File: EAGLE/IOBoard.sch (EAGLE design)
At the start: 71 parts, among them IC1 MEGA32-P, IC2 MAX232, IC3 ADM803SAKS, K1 HE3321, K2 HE3321, K3 HE3321, K4 HE3321, K5 HE3321, K6 HE3321, K7 HE3321, K8 HE3321, T1 NDS351AN, T2 NDS351AN, T3 NDS351AN, T4 NDS351AN, T5 NDS351AN, T6 NDS351AN, T7 NDS351AN, T8 NDS351AN

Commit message: -
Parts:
- removed D1, D2, D3, D4, D5, D6, D7, D8: 1N4148, diode:1N4148DO35-10
- removed IC2: MAX232, maxim:MAX232
- removed IC3: ADM803SAKS, memmert_joerg:ADM803SAKS
- removed K1, K2, K3, K4, K5, K6, K7, K8: HE3321, relay:HE3321
- removed OK1, OK2, OK3, OK4, OK5, OK6, OK7, OK8: SFH6206, optocoupler:SFH6206
- removed R10, R11, R12, R13, R14, R15, R16: 374, rcl:R-EU_0207/10
- removed T1, T2, T3, T4, T5, T6, T7, T8: NDS351AN, memmert_joerg:NDS351AN
- removed X1, X10, X11, X12, X13, X14, X15, X16, X2, X3, X4, X5, X6, X7, X8, X9: (no value), con-phoenix-500:MSTBV2
- removed X17: (no value), con-subd:F09H
- added 3V3, BAT: (no value), pinhead:PINHD-1X2
- added C3, C4, C5: 100n, rcl:C-EUC0805
- added C6, C7, C8, C9: 20p, rcl:C-EUC0805
- added JP1: (no value), pinhead:PINHD-1X9
- added JP10, JP11, JP2, JP3, JP4, JP5, JP6, JP7, JP8, JP9: JUMPER_SMALL, memmert_joerg:JUMPER_SMALL
- added JTAG: (no value), con-harting-ml:ML20
- added LED1, LED2, LED3, LED4: (no value), led:LEDSML0603
- added Q2: 32kHz, crystal:MC-306
- added S1: COMBICON_1803442, memmert_joerg:COMBICON_1803442
- added U1: STM32F10XRXT6, stm32:STM32F10XRXT6
- C1, C2: value (none) -> 100n; device rcl:C-EU025_050-025X075 -> rcl:C-EUC0805
- IC1: value MEGA32-P -> TPS61097; device atmel:MEGA32-P -> spfennig:TPS61097
- Q1: value (none) -> 8MHz; device memmert_joerg:CRYSTALHC49S -> crystal:CSM-7X-DU
- R1: value 5k -> 390; device rcl:R-EU_0207/10 -> rcl:R-EU_R0805
- R2, R3, R4: value 5k -> 10k; device rcl:R-EU_0207/10 -> rcl:R-EU_R0805
- R5: value 5k -> 0; device rcl:R-EU_0207/10 -> rcl:R-EU_R0805
- R6, R7, R8: value 5k -> 500; device rcl:R-EU_0207/10 -> rcl:R-EU_R0805
- R9: value 374 -> 500; device rcl:R-EU_0207/10 -> rcl:R-EU_R0805
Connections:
- removed net IN0: IC1.(ADC0)PA0, OK1.C, R1.1
- removed net IN1: IC1.(ADC1)PA1, OK2.C, R2.1
- removed net IN2: IC1.(ADC2)PA2, OK3.C, R3.1
- removed net IN3: IC1.(ADC3)PA3, OK4.C, R4.1
- removed net IN4: IC1.(ADC4)PA4, OK5.C, R5.1
- removed net IN5: IC1.(ADC5)PA5, OK6.C, R6.1
- removed net IN6: IC1.(ADC6)PA6, OK7.C, R7.1
- removed net IN7: IC1.(ADC7)PA7, OK8.C, R8.1
- removed net N$15: OK3.AC1, R11.2
- removed net N$16: C2.2, IC2G$1.C2-
- removed net N$17: R13.1, X5-1.SK
- removed net N$18: OK5.AC2, X5-2.SK
- removed net N$19: D1.A, K11.2, T1.D
- removed net N$20: OK5.AC1, R13.2
- removed net N$21: R14.1, X6-1.SK
- removed net N$22: OK6.AC2, X6-2.SK
- removed net N$23: IC1.RESET, IC3.!RESET
- removed net N$24: OK6.AC1, R14.2
- removed net N$25: R15.1, X7-1.SK
- removed net N$26: OK7.AC2, X7-2.SK
- removed net N$27: D4.A, K21.2, T2.D
- removed net N$28: OK7.AC1, R15.2
- removed net N$29: R16.1, X8-1.SK
- removed net N$30: OK8.AC2, X8-2.SK
- removed net N$31: D5.A, K31.2, T3.D
- removed net N$32: OK8.AC1, R16.2
- removed net N$33: D7.A, K41.2, T4.D
- removed net N$34: D2.A, K51.2, T5.D
- removed net N$35: D3.A, K61.2, T6.D
- removed net N$36: D8.A, K81.2, T8.D
- removed net N$37: D6.A, K71.2, T7.D
- removed net N$38: K12.S, X9-2.SK
- removed net N$39: K12.P, X9-1.SK
- removed net N$40: K22.S, X10-2.SK
- removed net N$41: K22.P, X10-1.SK
- removed net N$42: K32.S, X11-2.SK
- removed net N$43: K32.P, X11-1.SK
- removed net N$44: K42.S, X12-2.SK
- removed net N$45: K42.P, X12-1.SK
- removed net N$46: K82.S, X16-2.SK
- removed net N$47: K82.P, X16-1.SK
- removed net N$48: K72.P, X15-1.SK
- removed net N$49: K72.S, X15-2.SK
- removed net N$50: K62.P, X14-1.SK
- removed net N$51: K62.S, X14-2.SK
- removed net N$52: K52.P, X13-1.SK
- removed net N$53: K52.S, X13-2.SK
- removed net N$54: IC2G$1.T2OUT, X17.3
- removed net N$55: IC2G$1.R1IN, X17.2
- removed net N$56: IC1.XTAL2, Q1.2
- removed net N$57: IC1.XTAL1, Q1.1
- removed net OUT0: IC1.(T0/XCK)PB0, T1.G
- removed net OUT1: IC1.(T1)PB1, T2.G
- removed net OUT2: IC1.(AIN0/INT2)PB2, T3.G
- removed net OUT3: IC1.(AIN1/OC0)PB3, T4.G
- removed net OUT4: IC1.(SS)PB4, T5.G
- removed net OUT5: IC1.(MOSI)PB5, T6.G
- removed net OUT6: IC1.(MISO)PB6, T7.G
- removed net OUT7: IC1.(SCK)PB7, T8.G
- removed net RXUART: IC1.(RXD)PD0
- removed net TCK: IC1.(TCK)PC2
- removed net TDI: IC1.(TDI)PC5
- removed net TDO: IC1.(TDO)PC4
- removed net TMS: IC1.(TMS)PC3
- removed net TXUART: IC1.(TXD)PD1
- removed net VCC: D1.C, D2.C, D3.C, D4.C, D5.C, D6.C, D7.C, D8.C, IC1.AREF, IC1.AVCC, IC1.VCC, IC2G$1.V+, IC3.VCC, K11.1, K21.1, K31.1, K41.1, K51.1, K61.1, K71.1, K81.1, R1.2, R2.2, R3.2, R4.2, R5.2, R6.2, R7.2, R8.2
- new net +3V3: 3V3.1, C1.2, C2.2, C3.2, C4.2, IC1.VOUT, JP1.2, JP1.9, JP10.2, JP8.2, JTAG.1, JTAG.2, S1.3, U1AN_POWER.VBAT, U1AN_POWER.VDDA, U1POWER.VDD_1, U1POWER.VDD_2, U1POWER.VDD_3, U1POWER.VDD_4
- new net BAT+: BAT.1, IC1.EN, IC1.VIN
- new net BAT-: BAT.2, IC1.GND
- new net BOOT0: JP10.1, JP11.1, U1RESET.BOOT0
- new net BOOT1: JP8.1, JP9.1, U1PORTB_L.PB2
- new net JTAG_DBGACK: JTAG.19, R4.2
- new net JTAG_DBGRQ: JTAG.17, R3.2
- new net JTAG_NSRST: JP7.2, JTAG.15
- new net JTAG_NTRST: JP3.2, JTAG.3
- new net JTAG_RTCK: JTAG.11, R2.2
- new net JTAG_TCK: JP4.2, JTAG.9
- new net JTAG_TDI: JP5.2, JTAG.5
- new net JTAG_TDO: JP2.2, JTAG.13
- new net JTAG_TMS: JP6.2, JTAG.7
- new net LCD_CS: JP1.7, U1PORTB_L.PB6
- new net LCD_D/C: JP1.5, U1PORTA_H.PA8
- new net LCD_MISO: JP1.1, U1PORTA_L.PA6
- new net LCD_MOSI: JP1.4, U1PORTA_L.PA7
- new net LCD_RESET: JP1.6, U1PORTC_L.PC7
- new net LCD_SCK: JP1.3, U1PORTA_L.PA5
- new net OSC_RTC_IN: C8.1, Q2.2, U1PORTB_H.PB14
- new net OSC_RTC_OUT: R5.1, U1PORTB_H.PB15
- new net SERIAL1_RX: S1.2, U1PORTA_H.PA10
- new net SERIAL1_TX: S1.1, U1PORTA_H.PA9
- new net TEST_1: LED1.A, U1PORTA_L.PA3
- new net TEST_2: LED2.A, U1PORTA_L.PA2
- new net TEST_3: LED3.A, U1PORTA_L.PA1
- new net TEST_4: LED4.A, U1PORTA_L.PA0
- net GND: now also 3V3.2, C1.1, C2.1, C3.1, C4.1, C5.2, C6.2, C7.1, C8.2, C9.1, JP1.8, JP11.2, JP9.2, JTAG.10, JTAG.12, JTAG.14, JTAG.16, JTAG.18, JTAG.20, JTAG.4, JTAG.6, JTAG.8, R2.1, R3.1, R4.1, R6.1, R7.1, R8.1, R9.1, S1.4, U1AN_POWER.VSSA, U1POWER.VSS_1, U1POWER.VSS_2, U1POWER.VSS_3, U1POWER.VSS_4; no longer IC1.GND, IC1.GND@1, IC2G$1.V-, IC3.GND, OK1.E, OK2.E, OK3.E, OK4.E, OK5.E, OK6.E, OK7.E, OK8.E, T1.S, T2.S, T3.S, T4.S, T5.S, T6.S, T7.S, T8.S, X17.5
- net N$1: now also C5.1, JP7.1, U1RESET.NRST; no longer R9.1, X1-1.SK
- net N$10: now also C9.2, Q2.1, R5.2; no longer OK4.AC2, X4-2.SK
- net N$11: now also LED1.C, R6.2; no longer C2.1, IC2G$1.C2+
- net N$12: now also LED2.C, R7.2; no longer OK3.AC2, X3-2.SK
- net N$13: now also LED3.C, R8.2; no longer R12.1, X4-1.SK
- net N$14: now also LED4.C, R9.2; no longer OK4.AC1, R12.2
- net N$2: now also C6.1, Q1.2, U1PORTD/OSC.PD0/OSC<=; no longer OK1.AC1, R9.2
- net N$3: now also R1.1, U1PORTD/OSC.PD1/OSC=>; no longer C1.1, IC2G$1.C1+
- net N$4: now also JP2.1, U1PORTB_L.PB3; no longer OK1.AC2, X1-2.SK
- net N$5: now also C7.2, Q1.1, R1.2; no longer R10.1, X2-1.SK
- net N$6: now also JP4.1, U1PORTA_H.PA14; no longer OK2.AC1, R10.2
- net N$7: now also JP6.1, U1PORTA_H.PA13; no longer OK2.AC2, X2-2.SK
- net N$8: now also JP5.1, U1PORTA_H.PA15; no longer C1.2, IC2G$1.C1-
- net N$9: now also JP3.1, U1PORTB_L.PB4; no longer R11.1, X3-1.SK
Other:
- note added: "JTAG"
- note added: "STM32F103"
- note removed: "Input / Output"
- note removed: "Input Ports"
- note removed: "MCU"
- note removed: "Output Ports"
- note removed: "UART -> RS232"

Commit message: -
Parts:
- added C10, C11: 10u, rcl:C-EUC0805
- added L2: 4u7, ipc-7351-inductor:INDUCTOR_2520
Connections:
- new net N$15: IC1.L, L2.2
- net +3V3: now also C11.2
- net BAT+: now also C10.2, L2.1
- net BAT-: now also C10.1
- net GND: now also C11.1
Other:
- moved on the sheet: IC1
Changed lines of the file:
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@@
 <layer number="97" name="Info" color="7" fill="1" visible="yes" active="yes"/>
 <layer number="98" name="Guide" color="6" fill="1" visible="yes" active="yes"/>
+<layer number="99" name="SpiceOrder" color="5" fill="1" visible="yes" active="yes"/>
 <layer number="100" name="Muster" color="7" fill="1" visible="no" active="no"/>
 <layer number="101" name="Patch_Top" color="12" fill="4" visible="yes" active="yes"/>
@@
 </variantdefs>
 <classes>
-<class number="0" name="default" width="0" drill="0">
+<class number="0" name="default" width="0.2" drill="0.4">
+<clearance class="0" value="0.2"/>
 </class>
 </classes>
@@
 <part name="IC1" library="spfennig" deviceset="TPS61097" device=""/>
 <part name="+3V9" library="supply1" deviceset="+3V3" device=""/>
+<part name="L2" library="ipc-7351-inductor" deviceset="INDUCTOR_" device="2520" value="4u7"/>
+<part name="C10" library="rcl" deviceset="C-EU" device="C0805" value="10u"/>
+<part name="C11" library="rcl" deviceset="C-EU" device="C0805" value="10u"/>
+<part name="GND14" library="supply1" deviceset="GND" device=""/>
 </parts>
 <sheets>
@@
 <instance part="+3V8" gate="G$1" x="248.92" y="142.24" rot="R90"/>
 <instance part="BAT" gate="G$1" x="269.24" y="127"/>
-<instance part="IC1" gate="G$1" x="187.96" y="127"/>
-<instance part="+3V9" gate="G$1" x="205.74" y="134.62" rot="R270"/>
+<instance part="IC1" gate="G$1" x="205.74" y="137.16"/>
+<instance part="+3V9" gate="G$1" x="228.6" y="144.78" rot="R270"/>
+<instance part="L2" gate="G$1" x="187.96" y="144.78" smashed="yes">
+<attribute name="NAME" x="185.42" y="148.59" size="1.778" layer="95"/>
+<attribute name="VALUE" x="190.5" y="148.59" size="1.778" layer="96"/>
+</instance>
+<instance part="C10" gate="G$1" x="185.42" y="134.62" smashed="yes" rot="R180">
+<attribute name="NAME" x="186.944" y="137.541" size="1.778" layer="95"/>
+<attribute name="VALUE" x="183.896" y="139.319" size="1.778" layer="96" rot="R180"/>
+</instance>
+<instance part="C11" gate="G$1" x="223.52" y="137.16" smashed="yes" rot="R180">
+<attribute name="NAME" x="225.044" y="140.081" size="1.778" layer="95"/>
+<attribute name="VALUE" x="221.996" y="141.859" size="1.778" layer="96" rot="R180"/>
+</instance>
+<instance part="GND14" gate="1" x="223.52" y="129.54"/>
 </instances>
 <busses>
@@
 <wire x1="266.7" y1="139.7" x2="259.08" y2="139.7" width="0.1524" layer="91"/>
 </segment>
+<segment>
+<pinref part="C11" gate="G$1" pin="1"/>
+<pinref part="GND14" gate="1" pin="GND"/>
+<wire x1="223.52" y1="134.62" x2="223.52" y2="132.08" width="0.1524" layer="91"/>
+</segment>
 </net>
 <net name="+3V3" class="0">
@@
 <pinref part="IC1" gate="G$1" pin="VOUT"/>
 <pinref part="+3V9" gate="G$1" pin="+3V3"/>
-<wire x1="200.66" y1="134.62" x2="203.2" y2="134.62" width="0.1524" layer="91"/>
+<wire x1="218.44" y1="144.78" x2="223.52" y2="144.78" width="0.1524" layer="91"/>
+<pinref part="C11" gate="G$1" pin="2"/>
+<wire x1="223.52" y1="144.78" x2="226.06" y2="144.78" width="0.1524" layer="91"/>
+<wire x1="223.52" y1="144.78" x2="223.52" y2="142.24" width="0.1524" layer="91"/>
+<junction x="223.52" y="144.78"/>
 </segment>
 </net>
@@
 </segment>
 <segment>
-<wire x1="177.8" y1="129.54" x2="175.26" y2="129.54" width="0.1524" layer="91"/>
+<wire x1="195.58" y1="139.7" x2="193.04" y2="139.7" width="0.1524" layer="91"/>
 <pinref part="IC1" gate="G$1" pin="VIN"/>
-<wire x1="175.26" y1="129.54" x2="172.72" y2="129.54" width="0.1524" layer="91"/>
-<wire x1="175.26" y1="129.54" x2="175.26" y2="124.46" width="0.1524" layer="91"/>
-<junction x="175.26" y="129.54"/>
+<wire x1="193.04" y1="139.7" x2="193.04" y2="134.62" width="0.1524" layer="91"/>
+<junction x="193.04" y="139.7"/>
 <pinref part="IC1" gate="G$1" pin="EN"/>
-<wire x1="175.26" y1="124.46" x2="177.8" y2="124.46" width="0.1524" layer="91"/>
+<wire x1="193.04" y1="134.62" x2="195.58" y2="134.62" width="0.1524" layer="91"/>
+<label x="177.8" y="139.7" size="1.778" layer="95" rot="R180" xref="yes"/>
+<wire x1="193.04" y1="139.7" x2="185.42" y2="139.7" width="0.1524" layer="91"/>
+<pinref part="L2" gate="G$1" pin="1"/>
+<wire x1="185.42" y1="139.7" x2="177.8" y2="139.7" width="0.1524" layer="91"/>
+<wire x1="182.88" y1="144.78" x2="177.8" y2="144.78" width="0.1524" layer="91"/>
+<wire x1="177.8" y1="144.78" x2="177.8" y2="139.7" width="0.1524" layer="91"/>
+<pinref part="C10" gate="G$1" pin="2"/>
+<junction x="185.42" y="139.7"/>
 </segment>
 </net>
@@
 </segment>
 <segment>
-<wire x1="177.8" y1="121.92" x2="172.72" y2="121.92" width="0.1524" layer="91"/>
+<wire x1="195.58" y1="132.08" x2="185.42" y2="132.08" width="0.1524" layer="91"/>
 <pinref part="IC1" gate="G$1" pin="GND"/>
-</segment>
-</net>
+<label x="177.8" y="132.08" size="1.778" layer="95" rot="R180" xref="yes"/>
+<pinref part="C10" gate="G$1" pin="1"/>
+<wire x1="185.42" y1="132.08" x2="177.8" y2="132.08" width="0.1524" layer="91"/>
+<junction x="185.42" y="132.08"/>
+</segment>
+</net>
+<net name="N$15" class="0">
+<segment>
+<pinref part="IC1" gate="G$1" pin="L"/>
+<pinref part="L2" gate="G$1" pin="2"/>
+<wire x1="195.58" y1="144.78" x2="193.04" y2="144.78" width="0.1524" layer="91"/>
+</segment>
+</net>

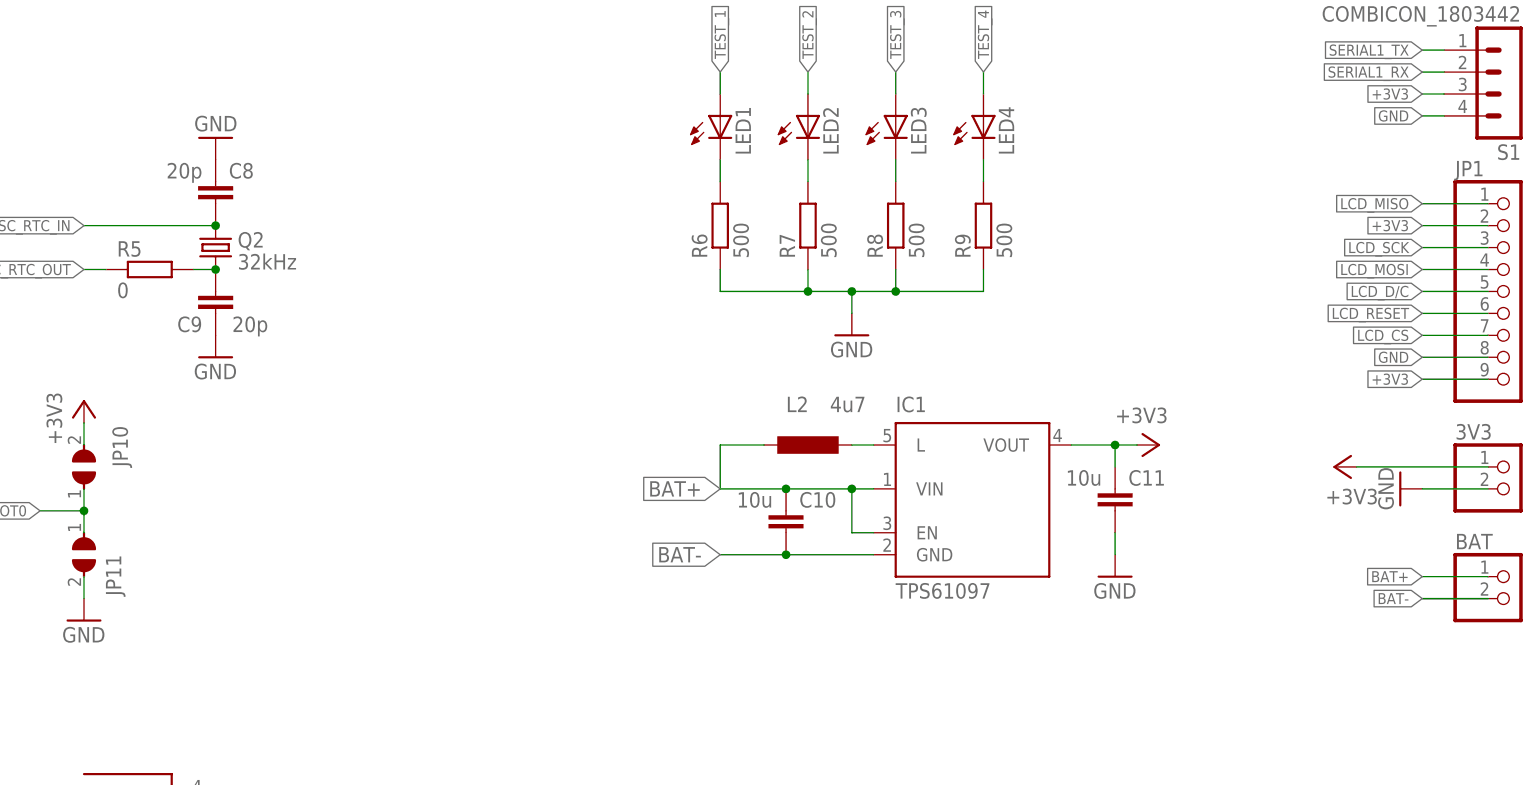
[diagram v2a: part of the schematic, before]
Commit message: Fixed bug with NAN
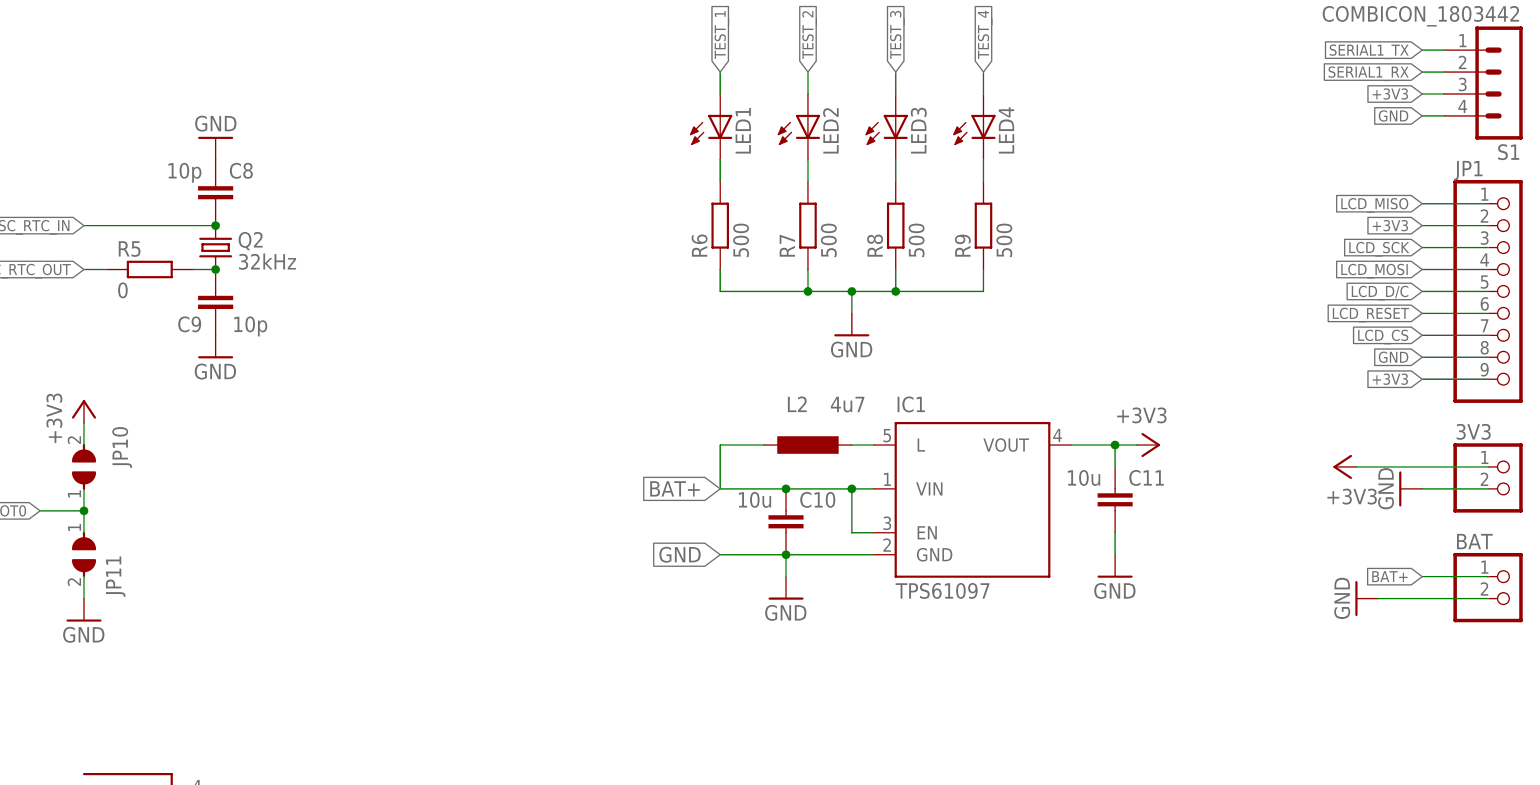
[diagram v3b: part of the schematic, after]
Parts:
- C8, C9: value 20p -> 10p
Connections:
- removed net BAT-: BAT.2, C10.1, IC1.GND
- net GND: now also BAT.2, C10.1, IC1.GND
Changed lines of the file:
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@@
 <part name="JP7" library="memmert_joerg" deviceset="JUMPER" device="_SMALL"/>
 <part name="Q2" library="crystal" deviceset="MC-306" device="" value="32kHz"/>
-<part name="C8" library="rcl" deviceset="C-EU" device="C0805" value="20p"/>
-<part name="C9" library="rcl" deviceset="C-EU" device="C0805" value="20p"/>
+<part name="C8" library="rcl" deviceset="C-EU" device="C0805" value="10p"/>
+<part name="C9" library="rcl" deviceset="C-EU" device="C0805" value="10p"/>
 <part name="GND8" library="supply1" deviceset="GND" device=""/>
 <part name="GND9" library="supply1" deviceset="GND" device=""/>
@@
 <part name="C11" library="rcl" deviceset="C-EU" device="C0805" value="10u"/>
 <part name="GND14" library="supply1" deviceset="GND" device=""/>
+<part name="GND15" library="supply1" deviceset="GND" device=""/>
+<part name="GND16" library="supply1" deviceset="GND" device=""/>
 </parts>
 <sheets>
@@
 </instance>
 <instance part="GND14" gate="1" x="223.52" y="129.54"/>
+<instance part="GND15" gate="1" x="185.42" y="127"/>
+<instance part="GND16" gate="1" x="251.46" y="127" rot="R270"/>
 </instances>
 <busses>
@@
 <wire x1="223.52" y1="134.62" x2="223.52" y2="132.08" width="0.1524" layer="91"/>
 </segment>
+<segment>
+<wire x1="195.58" y1="132.08" x2="185.42" y2="132.08" width="0.1524" layer="91"/>
+<pinref part="IC1" gate="G$1" pin="GND"/>
+<label x="177.8" y="132.08" size="1.778" layer="95" rot="R180" xref="yes"/>
+<pinref part="C10" gate="G$1" pin="1"/>
+<wire x1="185.42" y1="132.08" x2="177.8" y2="132.08" width="0.1524" layer="91"/>
+<junction x="185.42" y="132.08"/>
+<pinref part="GND15" gate="1" pin="GND"/>
+<wire x1="185.42" y1="132.08" x2="185.42" y2="129.54" width="0.1524" layer="91"/>
+</segment>
+<segment>
+<pinref part="BAT" gate="G$1" pin="2"/>
+<pinref part="GND16" gate="1" pin="GND"/>
+<wire x1="254" y1="127" x2="266.7" y2="127" width="0.1524" layer="91"/>
+</segment>
 </net>
 <net name="+3V3" class="0">
@@
 </segment>
 </net>
-<net name="BAT-" class="0">
-<segment>
-<pinref part="BAT" gate="G$1" pin="2"/>
-<wire x1="266.7" y1="127" x2="259.08" y2="127" width="0.1524" layer="91"/>
-<label x="259.08" y="127" size="1.27" layer="95" rot="R180" xref="yes"/>
-<wire x1="266.7" y1="127" x2="259.08" y2="127" width="0.1524" layer="91"/>
-</segment>
-<segment>
-<wire x1="195.58" y1="132.08" x2="185.42" y2="132.08" width="0.1524" layer="91"/>
-<pinref part="IC1" gate="G$1" pin="GND"/>
-<label x="177.8" y="132.08" size="1.778" layer="95" rot="R180" xref="yes"/>
-<pinref part="C10" gate="G$1" pin="1"/>
-<wire x1="185.42" y1="132.08" x2="177.8" y2="132.08" width="0.1524" layer="91"/>
-<junction x="185.42" y="132.08"/>
-</segment>
-</net>
